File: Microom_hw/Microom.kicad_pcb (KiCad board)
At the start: 2 copper layers, 144 parts, among them Q1 DVIUC6-4SC6, SW1 BUTTON

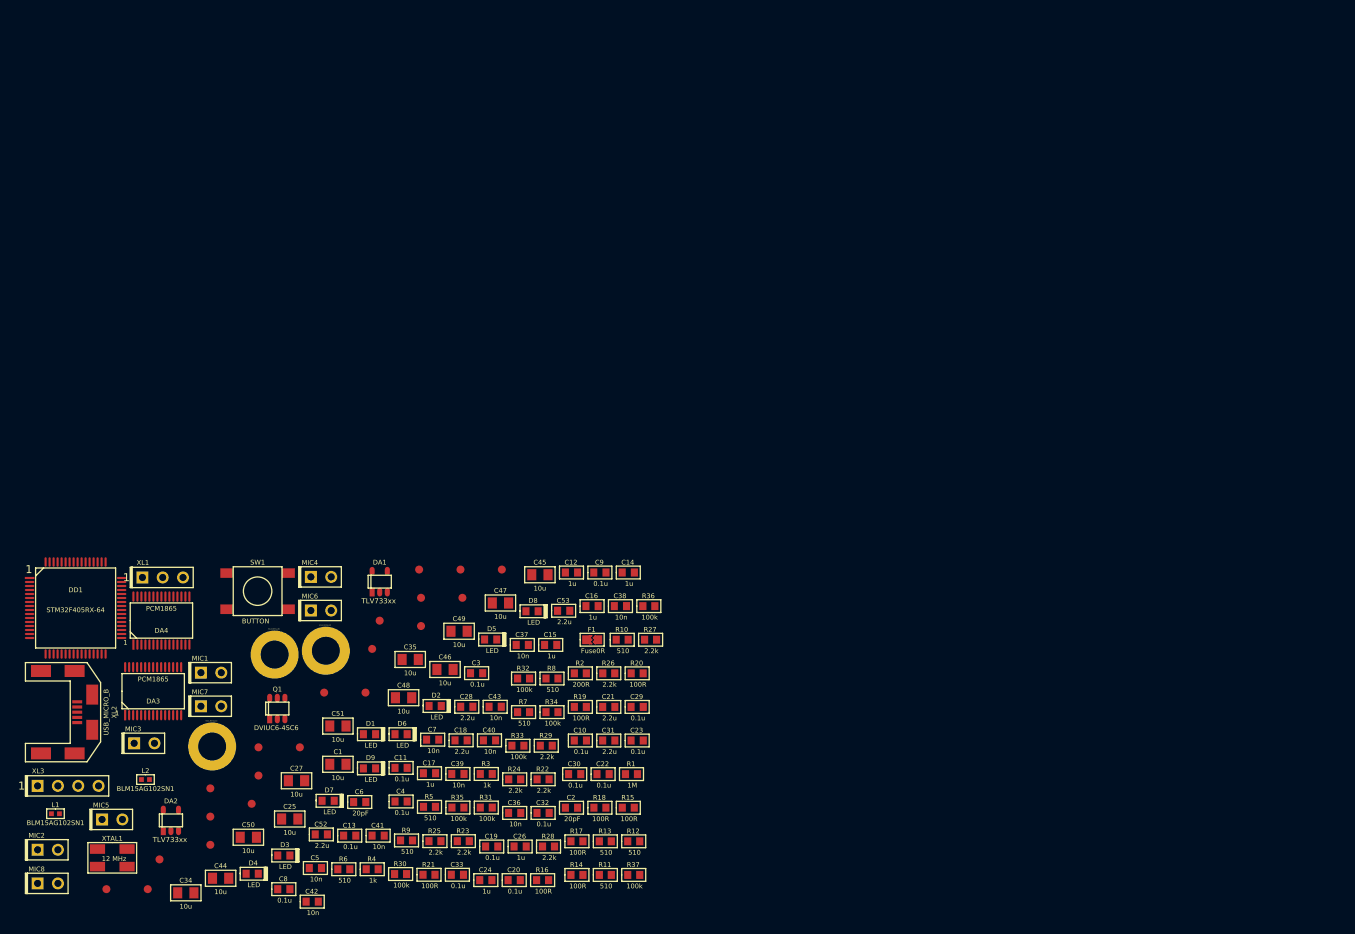
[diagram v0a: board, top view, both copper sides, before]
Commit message: * Components spread over the board
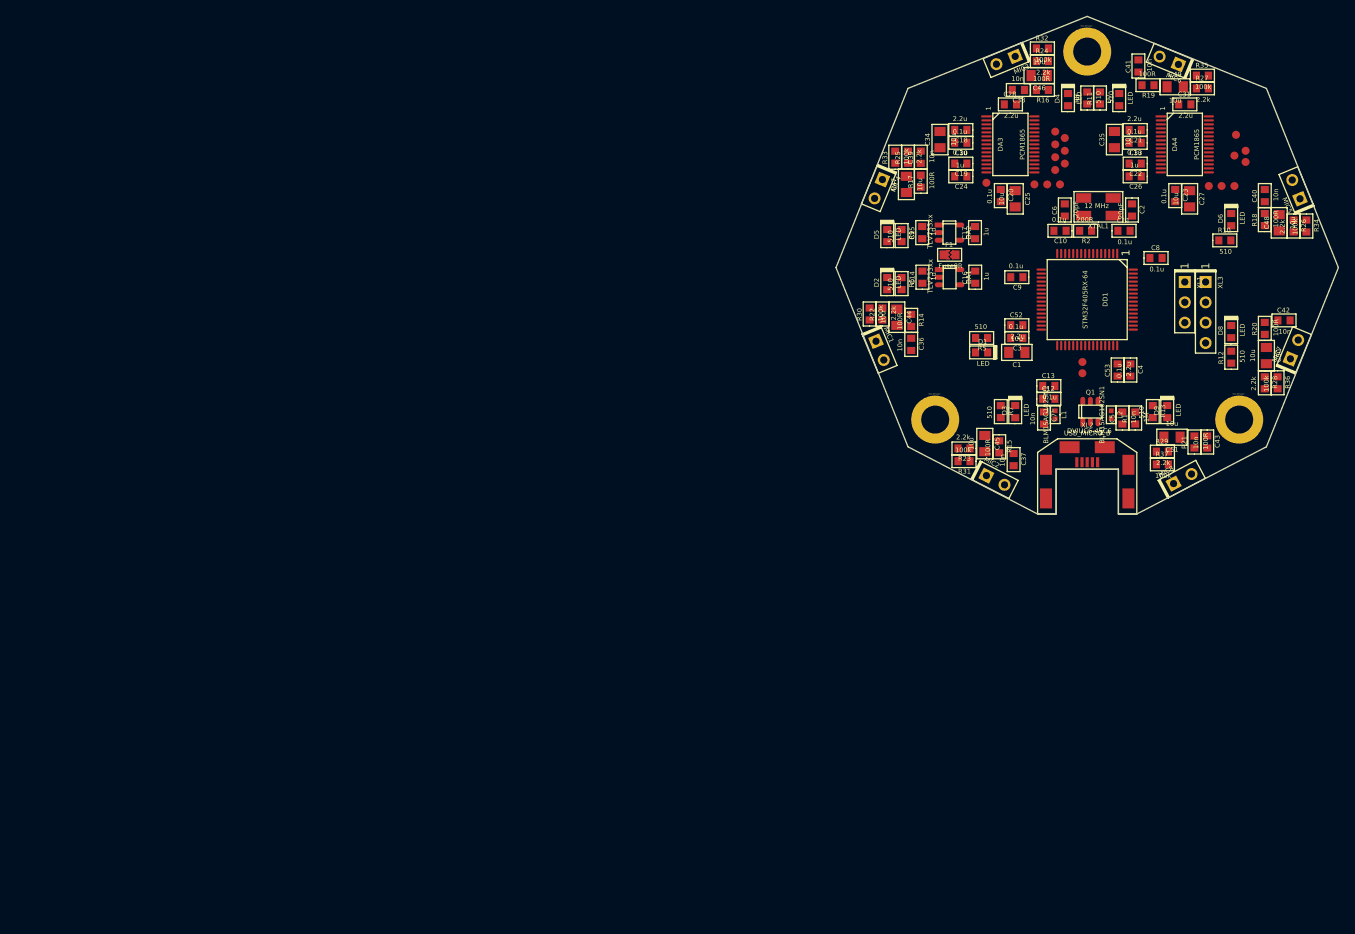
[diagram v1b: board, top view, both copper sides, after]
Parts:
- removed C29, C32: 0.1u, Capacitors:CAP_0603
- removed R3, R4: 1k, Resistors:RES_0603
- removed SW1: BUTTON, BtnsSwitches:BTN_6x6
- moved TP18 169.7 mm to (169.8, 94.4)
- moved MIC5 168.6 mm to (176.6, 100.4), turned to 112.5 degrees
- moved TP17 162.2 mm to (168.6, 92.4)
- moved XL3 159.0 mm to (164.8, 110.8), turned to 270 degrees
- moved TP20 151.3 mm to (169.8, 95.8)
- moved MIC8 150.5 mm to (160.8, 136.0), turned to 28 degrees
- moved XTAL1 147.7 mm to (151.4, 101.4), turned to 180 degrees
- moved TP6 144.1 mm to (146.6, 98.6)
- moved MIC7 142.9 mm to (175.4, 120.4), turned to 67.5 degrees
- moved TP16 142.5 mm to (168.4, 98.8)
- moved C42 141.5 mm to (174.6, 115.6)
- moved DA4 141.1 mm to (162.2, 93.6), turned to 270 degrees
- moved C50 140.8 mm to (172.4, 120.0), turned to 270 degrees
- moved D4 140.6 mm to (147.6, 88.0), turned to 90 degrees
- moved MIC3 139.6 mm to (141.0, 82.6), turned to 202.5 degrees
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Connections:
- DD1 pad 42: Net-(DD1-Pad42) -> +3.3V
- DD1 pad 60: Net-(DD1-Pad60) -> GND
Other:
- board outline added: 62.8 x 62.2 mm

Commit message: * PCB routing 30% completed
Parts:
- moved R8 14.4 mm to (135.6, 86.6), turned to 180 degrees
- moved D2 12.9 mm to (126.2, 123.8)
- moved R6 12.9 mm to (128.0, 123.8)
- moved R12 12.6 mm to (177.0, 111.4), turned to 270 degrees
- moved D4 12.4 mm to (135.6, 85.0), turned to 0 degrees
- moved R10 12.2 mm to (172.4, 94.6), turned to 90 degrees
- moved D6 10.3 mm to (174.0, 94.6), turned to 270 degrees
- moved D9 9.95 mm to (157.4, 136.6), turned to 270 degrees
- moved D8 9.37 mm to (177.0, 114.4), turned to 270 degrees
- moved D3 9.11 mm to (142.4, 136.0), turned to 270 degrees
- moved C1 7.61 mm to (140.8, 112.0)
- moved R7 6.80 mm to (142.4, 133.0)
- moved D7 6.71 mm to (155.2, 81.4), turned to 0 degrees
- moved R13 6.65 mm to (157.4, 133.6)
- moved R11 4.88 mm to (154.4, 83.8)
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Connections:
- C22 pad 1: /1V8 -> /1V8_2
- C26 pad 1: /1V8 -> /1V8_2
- D2 pad C: GND -> AGND
- D3 pad C: GND -> AGND
- D4 pad C: GND -> AGND
- D5 pad C: GND -> AGND
- D6 pad C: GND -> AGND
- D7 pad C: GND -> AGND
- D8 pad C: GND -> AGND
- D9 pad C: GND -> AGND
- DA4 pad 11: /1V8 -> /1V8_2
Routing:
- net AGND: track 0.00 -> 225.6 mm, vias 0 -> 13
- net GND: track 0.00 -> 83.7 mm, vias 0 -> 6
- net +3.3V: track 0.00 -> 76.4 mm, vias 0 -> 7
- net +3.3V_A: track 0.00 -> 51.9 mm, vias 0 -> 2
- net /MicBias: track 0.00 -> 48.4 mm, vias 0 -> 4
- net /VinR1: track 0.00 -> 46.4 mm, vias 0 -> 2
- net /SCK: track 0.00 -> 43.0 mm, vias 0 -> 4
- net /LED6: track 0.00 -> 37.9 mm, vias 0 -> 2
- net /VinL1: track 0.00 -> 30.6 mm, vias 0 -> 2
- net /SHLD: track 0.00 -> 29.8 mm, vias 0 -> 4
- net /GPIO11: track 0.00 -> 28.1 mm, vias 0 -> 2
- net /DataOut1: track 0.00 -> 25.2 mm
- net /SCKI: track 0.00 -> 24.9 mm, vias 0 -> 2
- net /BitClk1: track 0.00 -> 23.4 mm
- net /LRClk1: track 0.00 -> 22.1 mm
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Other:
- board size 62.8 x 62.2 mm -> 56.4 x 62.2 mm
- net class Default: trace_width 0.25 -> 0.2; via_dia 0.6 -> 0.8; via_drill 0.4 -> 0.3
- net class Wide added: clearance 0.2, trace_width 0.5, via_dia 0.8, via_drill 0.3

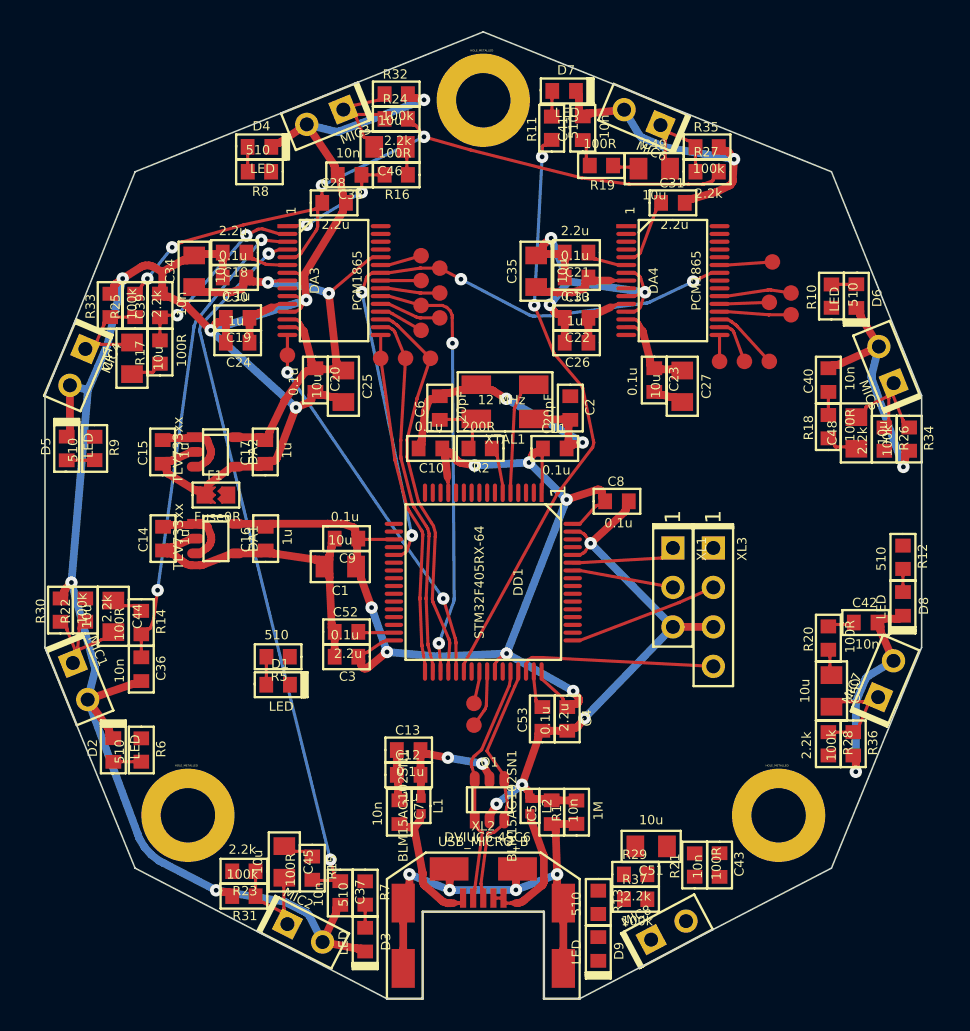
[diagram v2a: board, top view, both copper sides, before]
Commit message: Routing done, GND planes not placed yet.
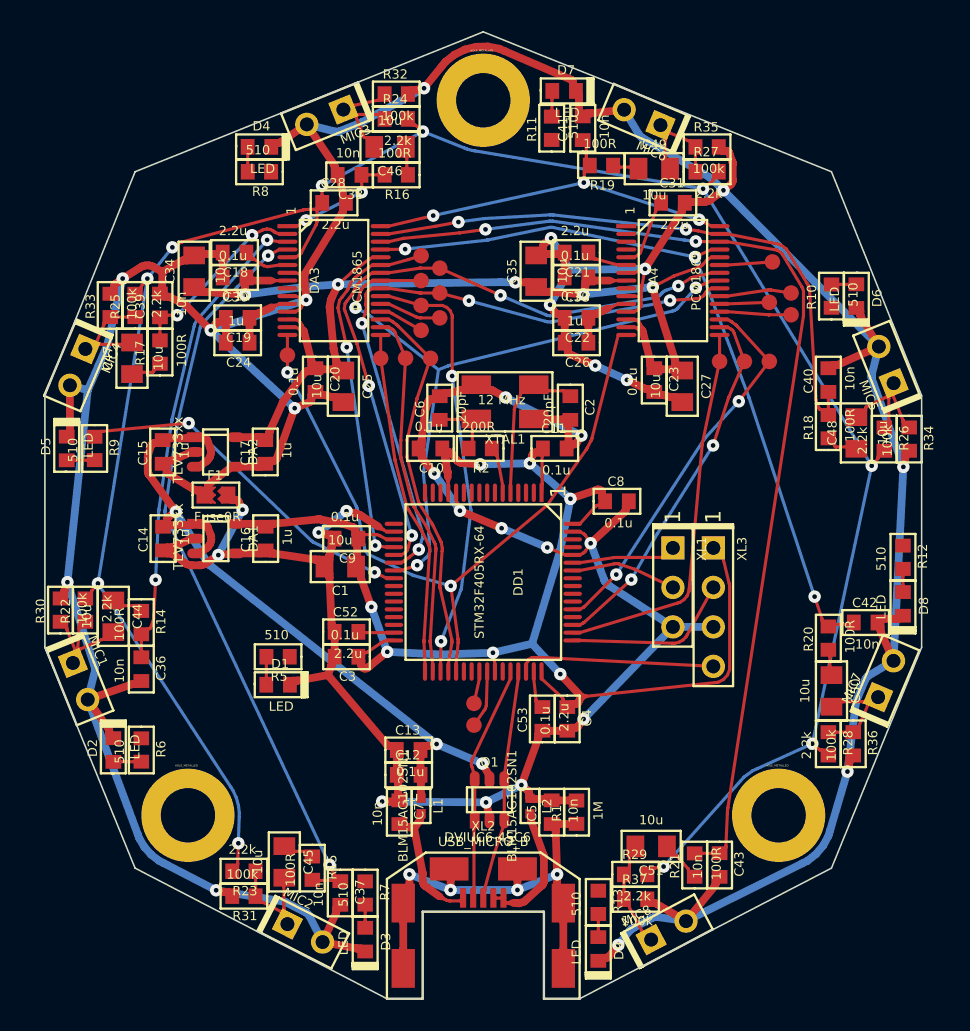
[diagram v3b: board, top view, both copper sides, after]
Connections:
- DD1 pad 10: /LED2 -> (no net)
- DD1 pad 11: /LED3 -> (no net)
- DD1 pad 14: /GPIO22 -> (no net)
- DD1 pad 15: /GPIO32 -> (no net)
- DD1 pad 17: /CS2 -> (no net)
- DD1 pad 2: /LED8 -> /CS2
- DD1 pad 25: /LED5 -> (no net)
- DD1 pad 28: (no net) -> /LED1
- DD1 pad 29: (no net) -> /LED_AUX
- DD1 pad 30: (no net) -> /LED2
- DD1 pad 38: /LED6 -> (no net)
- DD1 pad 39: /LED7 -> (no net)
- DD1 pad 43: (no net) -> /LED8
- DD1 pad 55: (no net) -> /GPIO32
- DD1 pad 56: (no net) -> /GPIO22
- DD1 pad 61: (no net) -> /LED5
- DD1 pad 62: (no net) -> /LED7
- DD1 pad 8: /LED_AUX -> /LED6
- DD1 pad 9: /LED1 -> /LED3
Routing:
- net /MicBias: track 48.4 -> 146.5 mm, vias 4 -> 10
- net AGND: track 225.6 -> 305.2 mm, vias 13 -> 16
- net /VinR4: track 0.00 -> 67.2 mm, vias 0 -> 2
- net /VinL4: track 1.68 -> 49.2 mm, vias 0 -> 3
- net GND: track 83.7 -> 129.1 mm, vias 6 -> 15
- net /MOSI: track 2.60 -> 45.8 mm, vias 0 -> 3
- net /MISO: track 3.82 -> 42.5 mm, vias 0 -> 4
- net /VinL3: track 1.49 -> 39.4 mm, vias 0 -> 2
- net /LED6: track 37.9 -> 0.00 mm, vias 2 -> 0
- net +3.3V_A: track 51.9 -> 82.8 mm, vias 2 -> 5
- net +5V: track 19.0 -> 49.0 mm, vias 2 -> 3
- net /VinR3: track 1.76 -> 25.6 mm, vias 0 -> 3
- net /LRClk2: track 1.70 -> 24.8 mm
- net /LED4: track 0.00 -> 23.0 mm, vias 0 -> 2
- net /SCKI: track 24.9 -> 47.2 mm
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
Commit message: + PCB completed and sent to production + BOM
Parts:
- moved HOLE1 0.50 mm to (150.0, 82.5)
- moved R26 0.13 mm to (175.7, 103.8)
- moved C40 0.13 mm to (172.1, 100.0)
- moved C48 0.13 mm to (173.9, 103.4)
- moved R18 0.13 mm to (172.1, 103.0)
- moved R34 0.13 mm to (177.3, 103.8)
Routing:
- net AGND: track 305.2 -> 488.5 mm, vias 16 -> 83
- net GND: track 129.1 -> 179.0 mm, vias 15 -> 38
- net /LED3: track 0.00 -> 31.7 mm, vias 0 -> 4
- net /GPIO12: track 4.65 -> 31.5 mm, vias 0 -> 2
- net /LED5: track 0.00 -> 26.8 mm, vias 0 -> 4
- net /LED6: track 0.00 -> 25.9 mm, vias 0 -> 2
- net /LED7: track 0.00 -> 25.9 mm, vias 0 -> 2
- net /GPIO22: track 3.20 -> 25.8 mm, vias 0 -> 2
- net /GPIO21: track 4.00 -> 25.5 mm
- net /CS2: track 3.41 -> 24.9 mm, vias 0 -> 2
- net /GPIO32: track 4.61 -> 25.9 mm, vias 0 -> 2
- net /GPIO31: track 2.92 -> 22.4 mm, vias 0 -> 2
- net /LED1: track 0.00 -> 18.9 mm
- net /LED8: track 0.00 -> 18.2 mm, vias 0 -> 2
- net /LED2: track 0.00 -> 17.6 mm
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- added copper zone on B.Cu, net AGND
- added copper zone on F.Cu, net AGND
- added copper zone on B.Cu, net GND
- added copper zone on F.Cu, net GND
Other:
- rule pad_to_mask_clearance: 0 -> 0.1
